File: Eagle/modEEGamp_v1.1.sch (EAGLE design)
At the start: 112 parts, among them IC2 INA217P, IC204 TLC277P, IC4 INA217P, P1 20k, P203 20k, Q1 BC547, Q2 BC557, Q202 BC557, Q204 BC557, Q206 BC547, Q208 BC547, Q3 BC547, Q4 BC557

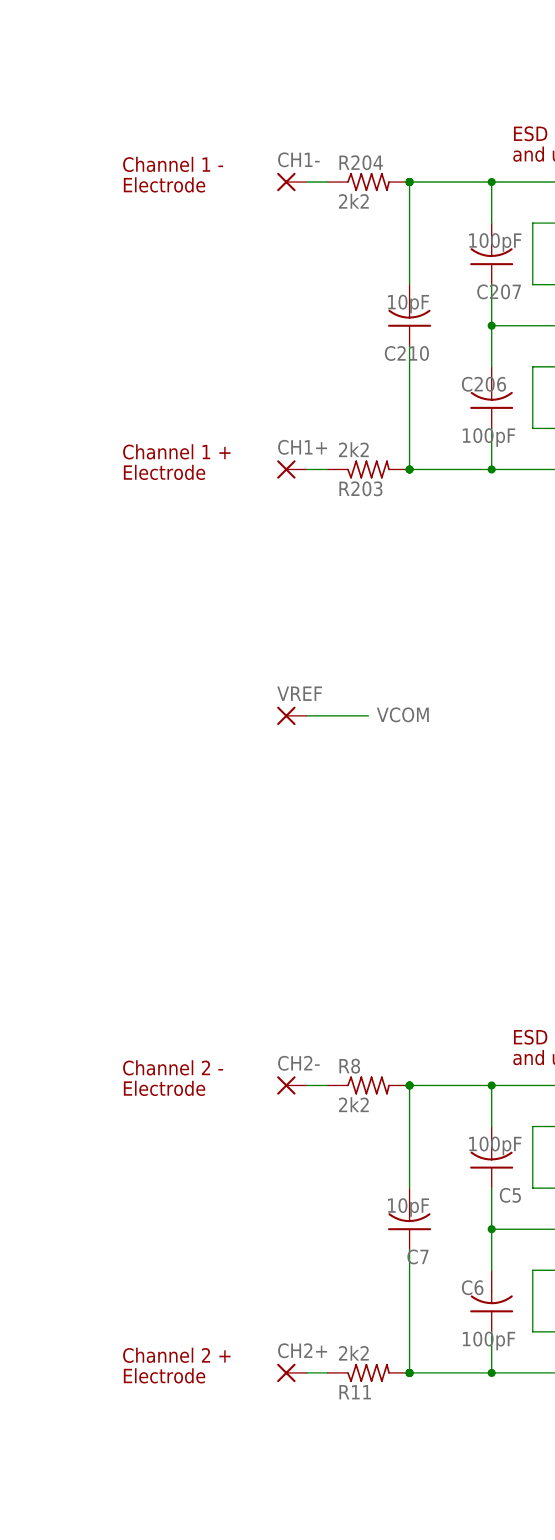
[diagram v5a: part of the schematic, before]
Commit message: Added DIN 42802 jacks & power for active electrodes
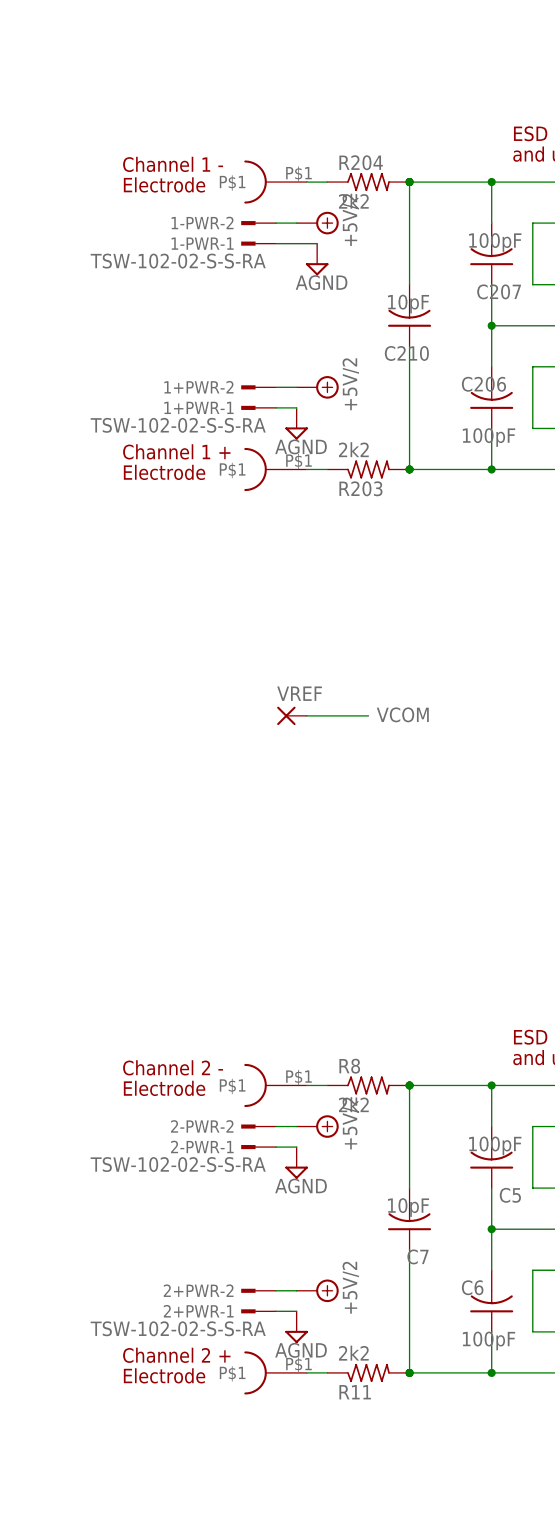
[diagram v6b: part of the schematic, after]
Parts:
- removed CH1+, CH1-, CH2+, CH2-: (no value), WIREPAD:1,6/0,8
- added 1+PWR, 1-PWR, 2+PWR, 2-PWR: TSW-102-02-S-S-RA, con-samtec:TSW-102-02-S-S-RA
- added C1+, C1-, C2+, C2-: DIN42802, modEEG:DIN42802
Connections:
- net +5V/2: now also 1+PWR-2.1, 1-PWR-2.1, 2+PWR-2.1, 2-PWR-2.1
- net AGND: now also 1+PWR-1.1, 1-PWR-1.1, 2+PWR-1.1, 2-PWR-1.1
- net N$11: now also C1+.P$1; no longer CH1+.P
- net N$24: now also C2-.P$1; no longer CH2-.P
- net N$26: now also C2+.P$1; no longer CH2+.P
- net N$6: now also C1-.P$1; no longer CH1-.P
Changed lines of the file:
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@@
 <part name="R217" library="resistor" deviceset="R-US_" device="0207/2V" value="2k2"/>
 <part name="R218" library="resistor" deviceset="R-US_" device="0207/2V" value="10k"/>
-<part name="CH1-" library="WIREPAD" deviceset="1,6/0,8" device="" value=" "/>
-<part name="CH1+" library="WIREPAD" deviceset="1,6/0,8" device="" value=" "/>
 <part name="U$26" library="SUPPLY2" deviceset="+5V/2" device=""/>
 <part name="C221" library="resistor" deviceset="C-US" device="C1206" value="1µF"/>
@@
 <part name="R5" library="resistor" deviceset="R-US_" device="0207/2V" value="2k2"/>
 <part name="R6" library="resistor" deviceset="R-US_" device="0207/2V" value="10k"/>
-<part name="CH2-" library="WIREPAD" deviceset="1,6/0,8" device="" value=" "/>
-<part name="CH2+" library="WIREPAD" deviceset="1,6/0,8" device="" value=" "/>
 <part name="U$22" library="SUPPLY2" deviceset="+5V/2" device=""/>
 <part name="C2" library="resistor" deviceset="C-US" device="C1206" value="1µF"/>
@@
 <part name="U$11" library="SUPPLY2" deviceset="AGND" device=""/>
 <part name="IC1" library="v-reg-micrel" deviceset="MIC5219XX" device=""/>
+<part name="C1-" library="modEEG" deviceset="DIN42802" device=""/>
+<part name="C1+" library="modEEG" deviceset="DIN42802" device=""/>
+<part name="C2-" library="modEEG" deviceset="DIN42802" device=""/>
+<part name="C2+" library="modEEG" deviceset="DIN42802" device=""/>
+<part name="1-PWR" library="con-samtec" deviceset="TSW-102-02-S-S" device="-RA"/>
+<part name="1+PWR" library="con-samtec" deviceset="TSW-102-02-S-S" device="-RA"/>
+<part name="2-PWR" library="con-samtec" deviceset="TSW-102-02-S-S" device="-RA"/>
+<part name="2+PWR" library="con-samtec" deviceset="TSW-102-02-S-S" device="-RA"/>
+<part name="U$12" library="SUPPLY2" deviceset="+5V/2" device=""/>
+<part name="U$14" library="SUPPLY2" deviceset="+5V/2" device=""/>
+<part name="U$25" library="SUPPLY2" deviceset="+5V/2" device=""/>
+<part name="U$27" library="SUPPLY2" deviceset="+5V/2" device=""/>
+<part name="U$38" library="SUPPLY2" deviceset="AGND" device=""/>
+<part name="U$42" library="SUPPLY2" deviceset="AGND" device=""/>
+<part name="U$45" library="SUPPLY2" deviceset="AGND" device=""/>
+<part name="U$46" library="SUPPLY2" deviceset="AGND" device=""/>
 </parts>
 <sheets>
@@
 <attribute name="VALUE" x="86.36" y="105.41" size="1.778" layer="96"/>
 </instance>
-<instance part="CH1-" gate="P" x="27.94" y="172.72"/>
-<instance part="CH1+" gate="P" x="27.94" y="137.16"/>
 <instance part="U$26" gate="G$1" x="167.64" y="170.18"/>
 <instance part="C221" gate="G$1" x="185.42" y="157.48" rot="R270"/>
@@
 <attribute name="VALUE" x="86.36" y="-6.35" size="1.778" layer="96"/>
 </instance>
-<instance part="CH2-" gate="P" x="27.94" y="60.96"/>
-<instance part="CH2+" gate="P" x="27.94" y="25.4"/>
 <instance part="U$22" gate="G$1" x="167.64" y="58.42"/>
 <instance part="C2" gate="G$1" x="185.42" y="45.72" rot="R270"/>
@@
 <instance part="IC1" gate="G1" x="490.22" y="116.84" rot="MR0"/>
 <instance part="IC204" gate="A" x="109.22" y="-2.54" rot="MR0"/>
+<instance part="C1-" gate="G$1" x="30.48" y="172.72" rot="R180"/>
+<instance part="C1+" gate="G$1" x="30.48" y="137.16" rot="R180"/>
+<instance part="C2-" gate="G$1" x="30.48" y="60.96" rot="R180"/>
+<instance part="C2+" gate="G$1" x="30.48" y="25.4" rot="R180"/>
+<instance part="1-PWR" gate="-1" x="24.13" y="165.1" rot="R180"/>
+<instance part="1-PWR" gate="-2" x="24.13" y="167.64" rot="R180"/>
+<instance part="1+PWR" gate="-1" x="24.13" y="144.78" rot="R180"/>
+<instance part="1+PWR" gate="-2" x="24.13" y="147.32" rot="R180"/>
+<instance part="2-PWR" gate="-1" x="24.13" y="53.34" rot="R180"/>
+<instance part="2-PWR" gate="-2" x="24.13" y="55.88" rot="R180"/>
+<instance part="2+PWR" gate="-1" x="24.13" y="33.02" rot="R180"/>
+<instance part="2+PWR" gate="-2" x="24.13" y="35.56" rot="R180"/>
+<instance part="U$12" gate="G$1" x="31.75" y="167.64" rot="R270"/>
+<instance part="U$14" gate="G$1" x="31.75" y="147.32" rot="R270"/>
+<instance part="U$25" gate="G$1" x="31.75" y="55.88" rot="R270"/>
+<instance part="U$27" gate="G$1" x="31.75" y="35.56" rot="R270"/>
+<instance part="U$38" gate="G$1" x="29.21" y="30.48"/>
+<instance part="U$42" gate="G$1" x="29.21" y="50.8"/>
+<instance part="U$45" gate="G$1" x="29.21" y="142.24"/>
+<instance part="U$46" gate="G$1" x="31.75" y="162.56"/>
 </instances>
 <busses>
@@
 <pinref part="U$44" gate="G$1" pin="AGND"/>
 </segment>
+<segment>
+<pinref part="2+PWR" gate="-1" pin="1"/>
+<pinref part="U$38" gate="G$1" pin="AGND"/>
+<wire x1="29.21" y1="33.02" x2="26.67" y2="33.02" width="0.1524" layer="91"/>
+</segment>
+<segment>
+<pinref part="2-PWR" gate="-1" pin="1"/>
+<pinref part="U$42" gate="G$1" pin="AGND"/>
+<wire x1="29.21" y1="53.34" x2="26.67" y2="53.34" width="0.1524" layer="91"/>
+</segment>
+<segment>
+<pinref part="1+PWR" gate="-1" pin="1"/>
+<pinref part="U$45" gate="G$1" pin="AGND"/>
+<wire x1="29.21" y1="144.78" x2="26.67" y2="144.78" width="0.1524" layer="91"/>
+</segment>
+<segment>
+<pinref part="1-PWR" gate="-1" pin="1"/>
+<pinref part="U$46" gate="G$1" pin="AGND"/>
+<wire x1="31.75" y1="165.1" x2="26.67" y2="165.1" width="0.1524" layer="91"/>
+</segment>
 </net>
 <net name="VCOM" class="0">
@@
 <wire x1="500.38" y1="116.84" x2="500.38" y2="121.92" width="0.1524" layer="91"/>
 <junction x="500.38" y="121.92"/>
+</segment>
+<segment>
+<pinref part="1-PWR" gate="-2" pin="1"/>
+<pinref part="U$12" gate="G$1" pin="+5V/2"/>
+<wire x1="29.21" y1="167.64" x2="26.67" y2="167.64" width="0.1524" layer="91"/>
+</segment>
+<segment>
+<pinref part="1+PWR" gate="-2" pin="1"/>
+<pinref part="U$14" gate="G$1" pin="+5V/2"/>
+<wire x1="29.21" y1="147.32" x2="26.67" y2="147.32" width="0.1524" layer="91"/>
+</segment>
+<segment>
+<pinref part="2-PWR" gate="-2" pin="1"/>
+<pinref part="U$25" gate="G$1" pin="+5V/2"/>
+<wire x1="29.21" y1="55.88" x2="26.67" y2="55.88" width="0.1524" layer="91"/>
+</segment>
+<segment>
+<pinref part="2+PWR" gate="-2" pin="1"/>
+<pinref part="U$27" gate="G$1" pin="+5V/2"/>
+<wire x1="29.21" y1="35.56" x2="26.67" y2="35.56" width="0.1524" layer="91"/>
 </segment>
 </net>
@@
 <wire x1="30.48" y1="172.72" x2="33.02" y2="172.72" width="0.1524" layer="91"/>
 <pinref part="R204" gate="G$1" pin="1"/>
-<pinref part="CH1-" gate="P" pin="P"/>
+<pinref part="C1-" gate="G$1" pin="P$1"/>
 </segment>
 </net>
@@
 <wire x1="30.48" y1="137.16" x2="33.02" y2="137.16" width="0.1524" layer="91"/>
 <pinref part="R203" gate="G$1" pin="1"/>
-<pinref part="CH1+" gate="P" pin="P"/>
+<pinref part="C1+" gate="G$1" pin="P$1"/>
 </segment>
 </net>
@@
 <wire x1="30.48" y1="60.96" x2="33.02" y2="60.96" width="0.1524" layer="91"/>
 <pinref part="R8" gate="G$1" pin="1"/>
-<pinref part="CH2-" gate="P" pin="P"/>
+<pinref part="C2-" gate="G$1" pin="P$1"/>
 </segment>
 </net>
@@
 <wire x1="30.48" y1="25.4" x2="33.02" y2="25.4" width="0.1524" layer="91"/>
 <pinref part="R11" gate="G$1" pin="1"/>
-<pinref part="CH2+" gate="P" pin="P"/>
-</segment>
-</net>
+<pinref part="C2+" gate="G$1" pin="P$1"/>
+</segment>
+</net>

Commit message: Added indicator LEDs
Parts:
- added LED1, LED2: (no value), led:LED3MM
- added R1, R2: (no value), resistor:R-US_0207/2V
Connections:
- new net N$67: LED2.A, R2.1
- new net N$9: LED1.A, R1.1
- net +5V/2: now also R1.2
- net AGND: now also LED1.C, LED2.C
- net N$8: now also R2.2
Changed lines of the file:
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@@
 <part name="U$45" library="SUPPLY2" deviceset="AGND" device=""/>
 <part name="U$46" library="SUPPLY2" deviceset="AGND" device=""/>
+<part name="LED1" library="led" deviceset="LED" device="3MM"/>
+<part name="R1" library="resistor" deviceset="R-US_" device="0207/2V"/>
+<part name="U$47" library="SUPPLY2" deviceset="AGND" device=""/>
+<part name="R2" library="resistor" deviceset="R-US_" device="0207/2V"/>
+<part name="U$48" library="SUPPLY2" deviceset="AGND" device=""/>
+<part name="LED2" library="led" deviceset="LED" device="3MM"/>
 </parts>
 <sheets>
@@
 <instance part="U$45" gate="G$1" x="29.21" y="142.24"/>
 <instance part="U$46" gate="G$1" x="31.75" y="162.56"/>
+<instance part="LED1" gate="G$1" x="515.62" y="109.22"/>
+<instance part="R1" gate="G$1" x="515.62" y="116.84" rot="R90"/>
+<instance part="U$47" gate="G$1" x="515.62" y="101.6"/>
+<instance part="R2" gate="G$1" x="444.5" y="76.2" rot="R90"/>
+<instance part="U$48" gate="G$1" x="444.5" y="60.96"/>
+<instance part="LED2" gate="G$1" x="444.5" y="68.58"/>
 </instances>
 <busses>
@@
 <wire x1="31.75" y1="165.1" x2="26.67" y2="165.1" width="0.1524" layer="91"/>
 </segment>
+<segment>
+<pinref part="LED1" gate="G$1" pin="C"/>
+<pinref part="U$47" gate="G$1" pin="AGND"/>
+</segment>
+<segment>
+<pinref part="LED2" gate="G$1" pin="C"/>
+<pinref part="U$48" gate="G$1" pin="AGND"/>
+</segment>
 </net>
 <net name="VCOM" class="0">
@@
 <wire x1="500.38" y1="116.84" x2="500.38" y2="121.92" width="0.1524" layer="91"/>
 <junction x="500.38" y="121.92"/>
+<pinref part="R1" gate="G$1" pin="2"/>
+<wire x1="500.38" y1="121.92" x2="515.62" y2="121.92" width="0.1524" layer="91"/>
 </segment>
 <segment>
@@
 <junction x="444.5" y="88.9"/>
 <pinref part="X2" gate="-19" pin="F"/>
+<pinref part="R2" gate="G$1" pin="2"/>
+<junction x="444.5" y="81.28"/>
 </segment>
 </net>
@@
 </segment>
 </net>
+<net name="N$9" class="0">
+<segment>
+<pinref part="LED1" gate="G$1" pin="A"/>
+<pinref part="R1" gate="G$1" pin="1"/>
+</segment>
+</net>
+<net name="N$67" class="0">
+<segment>
+<pinref part="R2" gate="G$1" pin="1"/>
+<pinref part="LED2" gate="G$1" pin="A"/>
+</segment>
+</net>

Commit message: Updated resistor values
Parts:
- removed LED2: (no value), led:LED3MM
- removed R2: (no value), resistor:R-US_0207/2V
- R1: value (none) -> 1.65k
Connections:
- removed net N$67: LED2.A, R2.1
- net AGND: no longer LED2.C
- net N$8: no longer R2.2
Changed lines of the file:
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@@
 <part name="U$46" library="SUPPLY2" deviceset="AGND" device=""/>
 <part name="LED1" library="led" deviceset="LED" device="3MM"/>
-<part name="R1" library="resistor" deviceset="R-US_" device="0207/2V"/>
+<part name="R1" library="resistor" deviceset="R-US_" device="0207/2V" value="1.65k"/>
 <part name="U$47" library="SUPPLY2" deviceset="AGND" device=""/>
-<part name="R2" library="resistor" deviceset="R-US_" device="0207/2V"/>
-<part name="U$48" library="SUPPLY2" deviceset="AGND" device=""/>
-<part name="LED2" library="led" deviceset="LED" device="3MM"/>
 </parts>
 <sheets>
@@
 <instance part="R1" gate="G$1" x="515.62" y="116.84" rot="R90"/>
 <instance part="U$47" gate="G$1" x="515.62" y="101.6"/>
-<instance part="R2" gate="G$1" x="444.5" y="76.2" rot="R90"/>
-<instance part="U$48" gate="G$1" x="444.5" y="60.96"/>
-<instance part="LED2" gate="G$1" x="444.5" y="68.58"/>
 </instances>
 <busses>
@@
 <pinref part="LED1" gate="G$1" pin="C"/>
 <pinref part="U$47" gate="G$1" pin="AGND"/>
-</segment>
-<segment>
-<pinref part="LED2" gate="G$1" pin="C"/>
-<pinref part="U$48" gate="G$1" pin="AGND"/>
 </segment>
 </net>
@@
 <junction x="444.5" y="88.9"/>
 <pinref part="X2" gate="-19" pin="F"/>
-<pinref part="R2" gate="G$1" pin="2"/>
-<junction x="444.5" y="81.28"/>
 </segment>
 </net>
@@
 </segment>
 </net>
-<net name="N$67" class="0">
-<segment>
-<pinref part="R2" gate="G$1" pin="1"/>
-<pinref part="LED2" gate="G$1" pin="A"/>
-</segment>
-</net>
